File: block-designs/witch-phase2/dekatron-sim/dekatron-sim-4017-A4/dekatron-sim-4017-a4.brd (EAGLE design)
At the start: 27.9 x 27.9 mm, 19 parts, among them IC1 4017D, IC2 74LVC1G125DBV

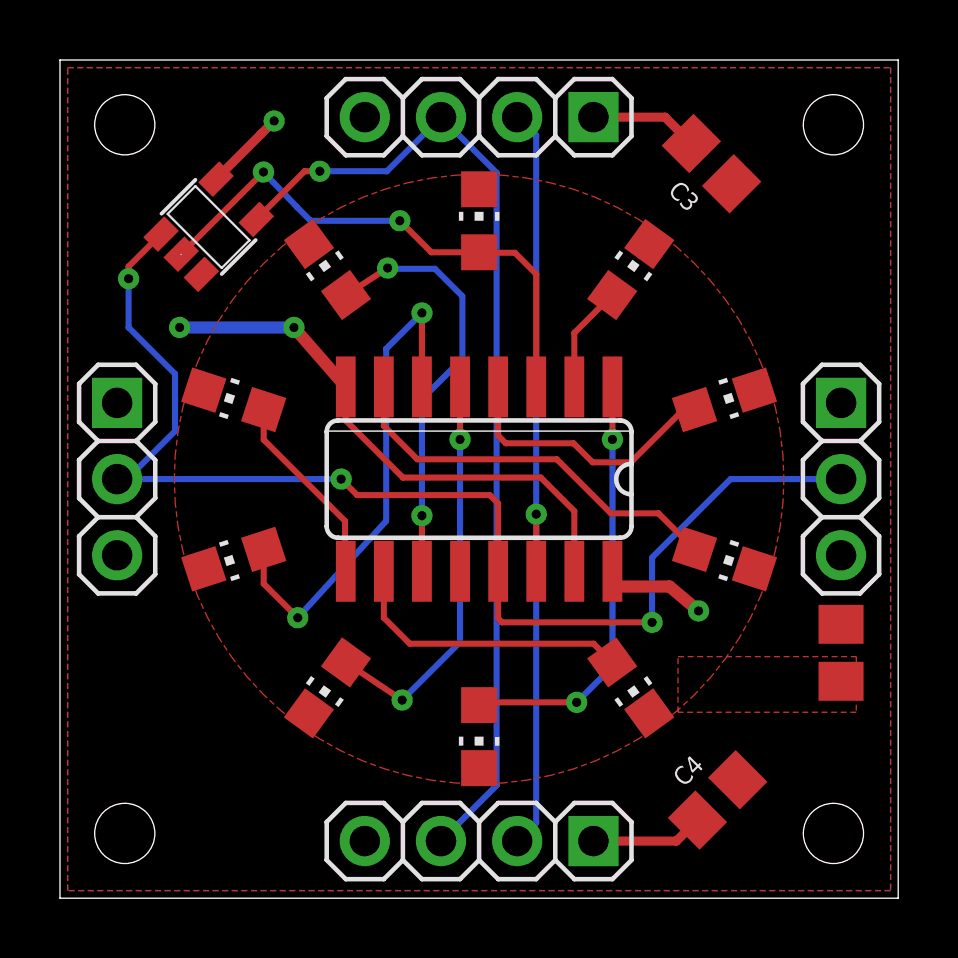
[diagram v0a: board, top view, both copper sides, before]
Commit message: updated designs for new labeling and spacing
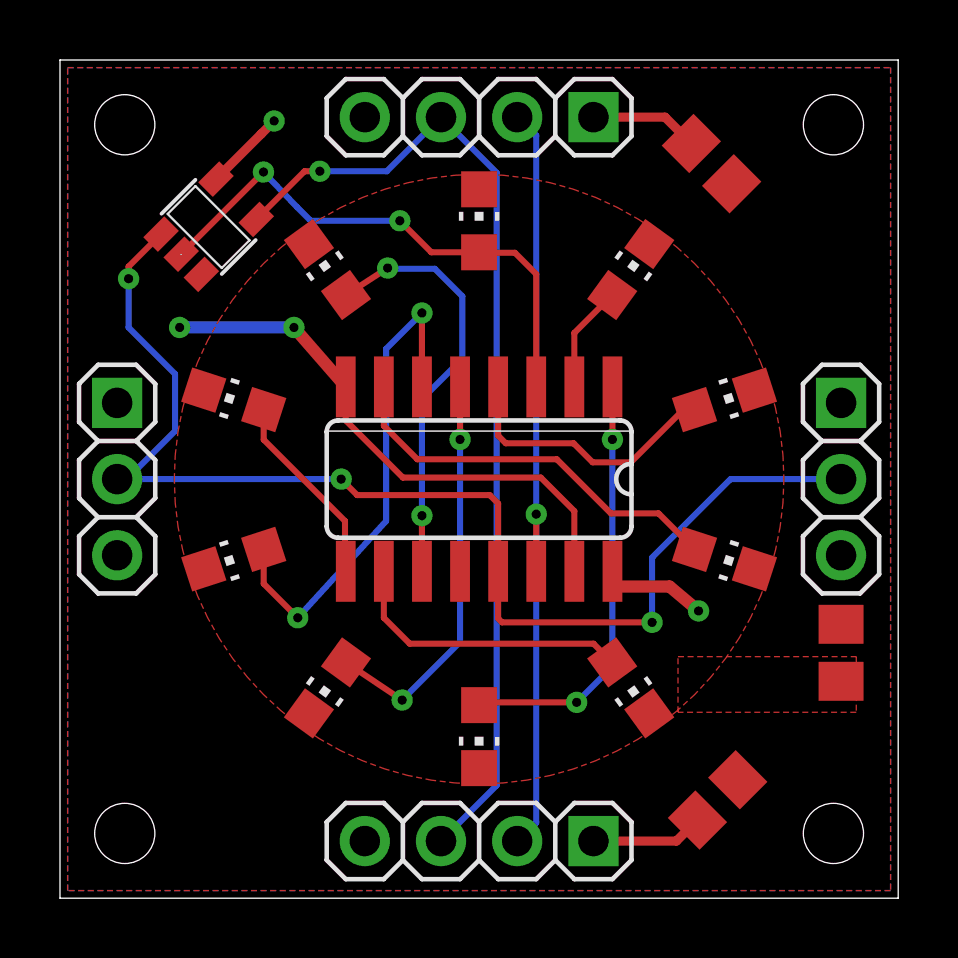
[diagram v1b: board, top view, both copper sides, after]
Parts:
- renumbered C3 to C1, C4 to C2, JP5 to JP1, JP6 to JP3
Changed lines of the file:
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@@
 <layer number="29" name="tStop" color="7" fill="3" visible="no" active="yes"/>
 <layer number="30" name="bStop" color="7" fill="6" visible="no" active="yes"/>
-<layer number="31" name="tCream" color="7" fill="4" visible="yes" active="yes"/>
+<layer number="31" name="tCream" color="7" fill="4" visible="no" active="yes"/>
 <layer number="32" name="bCream" color="7" fill="5" visible="no" active="yes"/>
 <layer number="33" name="tFinish" color="6" fill="3" visible="no" active="yes"/>
@@
 <wire x1="27.94" y1="0" x2="27.94" y2="27.94" width="0" layer="20"/>
 <circle x="13.97" y="13.97" radius="10.41994375" width="0.254" layer="51"/>
-<text x="13.5636" y="19.6342" size="1.016" layer="51">0</text>
-<text x="17.1958" y="18.6182" size="1.016" layer="51">1</text>
-<text x="19.5326" y="15.3416" size="1.016" layer="51">2</text>
-<text x="19.5326" y="11.3792" size="1.016" layer="51">3</text>
-<text x="17.1958" y="8.382" size="1.016" layer="51">4</text>
-<text x="13.5636" y="7.366" size="1.016" layer="51">5</text>
-<text x="10.0584" y="8.382" size="1.016" layer="51">6</text>
-<text x="7.6962" y="11.3792" size="1.016" layer="51">7</text>
-<text x="7.6962" y="15.3416" size="1.016" layer="51">8</text>
-<text x="10.0584" y="18.6182" size="1.016" layer="51">9</text>
+<text x="13.5636" y="19.558" size="1.016" layer="48">0</text>
+<text x="17.1958" y="18.415" size="1.016" layer="48">1</text>
+<text x="19.5326" y="15.3416" size="1.016" layer="48">2</text>
+<text x="19.5326" y="11.3792" size="1.016" layer="48">3</text>
+<text x="17.1958" y="8.509" size="1.016" layer="48">4</text>
+<text x="13.5636" y="7.493" size="1.016" layer="48">5</text>
+<text x="10.0584" y="8.509" size="1.016" layer="48">6</text>
+<text x="7.8232" y="11.3792" size="1.016" layer="48">7</text>
+<text x="7.8232" y="15.3416" size="1.016" layer="48">8</text>
+<text x="10.0584" y="18.415" size="1.016" layer="48">9</text>
 <hole x="2.159" y="2.159" drill="2.0066"/>
 <hole x="25.781" y="2.159" drill="2.0066"/>
@@
 <elements>
 <element name="IC1" library="40xx" package="SO16" value="4017D" x="13.97" y="13.97" smashed="yes" rot="R180">
-<attribute name="VALUE" x="9.745" y="17.22" size="0.6096" layer="27" rot="R270"/>
+<attribute name="VALUE" x="12.2948" y="13.7328" size="0.6096" layer="27"/>
 </element>
 <element name="LED1" library="led" package="CHIP-LED0805" value="RED" x="13.97" y="22.5806" smashed="yes"/>
@@
 <element name="LED9" library="led" package="CHIP-LED0805" value="RED" x="5.7912" y="16.6116" smashed="yes" rot="R72"/>
 <element name="LED10" library="led" package="CHIP-LED0805" value="RED" x="8.9154" y="20.955" smashed="yes" rot="R36"/>
-<element name="C3" library="resistor" package="C0805" value="" x="21.717" y="24.4856" smashed="yes" rot="R315">
-<attribute name="NAME" x="20.232003125" y="23.5466375" size="0.6096" layer="25" rot="R315"/>
+<element name="C1" library="resistor" package="C0805" value="" x="21.717" y="24.4856" smashed="yes" rot="R315">
 <attribute name="VALUE" x="19.4719375" y="23.49776875" size="1.27" layer="27" rot="R315"/>
 </element>
-<element name="C4" library="resistor" package="C0805" value="" x="21.9202" y="3.2766" smashed="yes" rot="R45">
-<attribute name="NAME" x="20.79621875" y="3.68035625" size="0.6096" layer="25" rot="R45"/>
+<element name="C2" library="resistor" package="C0805" value="" x="21.9202" y="3.2766" smashed="yes" rot="R45">
 <attribute name="VALUE" x="22.90803125" y="1.031534375" size="1.27" layer="27" rot="R45"/>
 </element>
 <element name="IC2" library="74xx-little-us" package="SOT23-5" value="74LVC1G125DBV" x="4.953" y="22.3774" smashed="yes" rot="R315">
-<attribute name="VALUE" x="1.360896875" y="22.377403125" size="1.27" layer="27" rot="R315"/>
+<attribute name="VALUE" x="4.927603125" y="25.004303125" size="0.3048" layer="27" rot="R225"/>
 </element>
 <element name="JP2" library="pinhead" package="1X04" value="" x="13.97" y="26.035" smashed="yes" rot="R180">
@@
 <attribute name="VALUE" x="23.494996875" y="8.8138" size="1.27" layer="27" rot="R270"/>
 </element>
-<element name="JP5" library="pinhead" package="1X03" value="" x="1.905" y="13.97" smashed="yes" rot="R270">
+<element name="JP1" library="pinhead" package="1X03" value="" x="1.905" y="13.97" smashed="yes" rot="R270">
 <attribute name="VALUE" x="-1.27" y="17.78" size="1.27" layer="27" rot="R270"/>
 </element>
-<element name="JP6" library="pinhead" package="1X03" value="" x="26.035" y="13.97" smashed="yes" rot="R270">
+<element name="JP3" library="pinhead" package="1X03" value="" x="26.035" y="13.97" smashed="yes" rot="R270">
 <attribute name="VALUE" x="22.86" y="17.78" size="1.27" layer="27" rot="R270"/>
 </element>
@@
 <signals>
 <signal name="GND">
-<contactref element="C3" pad="2"/>
-<contactref element="C4" pad="2"/>
+<contactref element="C1" pad="2"/>
+<contactref element="C2" pad="2"/>
 <contactref element="JP2" pad="4"/>
 <contactref element="JP4" pad="4"/>
@@
 </polygon>
 <contactref element="R1" pad="1"/>
-<contactref element="JP5" pad="3"/>
-<contactref element="JP6" pad="3"/>
+<contactref element="JP1" pad="3"/>
+<contactref element="JP3" pad="3"/>
 <contactref element="IC2" pad="3"/>
 <contactref element="IC1" pad="8"/>
@@
 <contactref element="IC1" pad="13"/>
 <contactref element="IC2" pad="1"/>
-<contactref element="JP5" pad="2"/>
-<contactref element="JP6" pad="2"/>
+<contactref element="JP1" pad="2"/>
+<contactref element="JP3" pad="2"/>
 <via x="2.286" y="20.6502" extent="1-16" drill="0.3048"/>
 <wire x1="2.7178" y1="13.97" x2="1.905" y2="13.97" width="0.2032" layer="16"/>
@@
 <signal name="VCC">
 <contactref element="IC2" pad="5"/>
-<contactref element="C4" pad="1"/>
-<contactref element="C3" pad="1"/>
+<contactref element="C2" pad="1"/>
+<contactref element="C1" pad="1"/>
 <polygon width="0.254" layer="16">
 <vertex x="27.686" y="0.254"/>
@@
 <vertex x="27.686" y="27.686"/>
 </polygon>
-<contactref element="JP5" pad="1"/>
-<contactref element="JP6" pad="1"/>
+<contactref element="JP1" pad="1"/>
+<contactref element="JP3" pad="1"/>
 <contactref element="JP2" pad="1"/>
 <contactref element="JP4" pad="1"/>

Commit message: add fiducials for pick-and-place
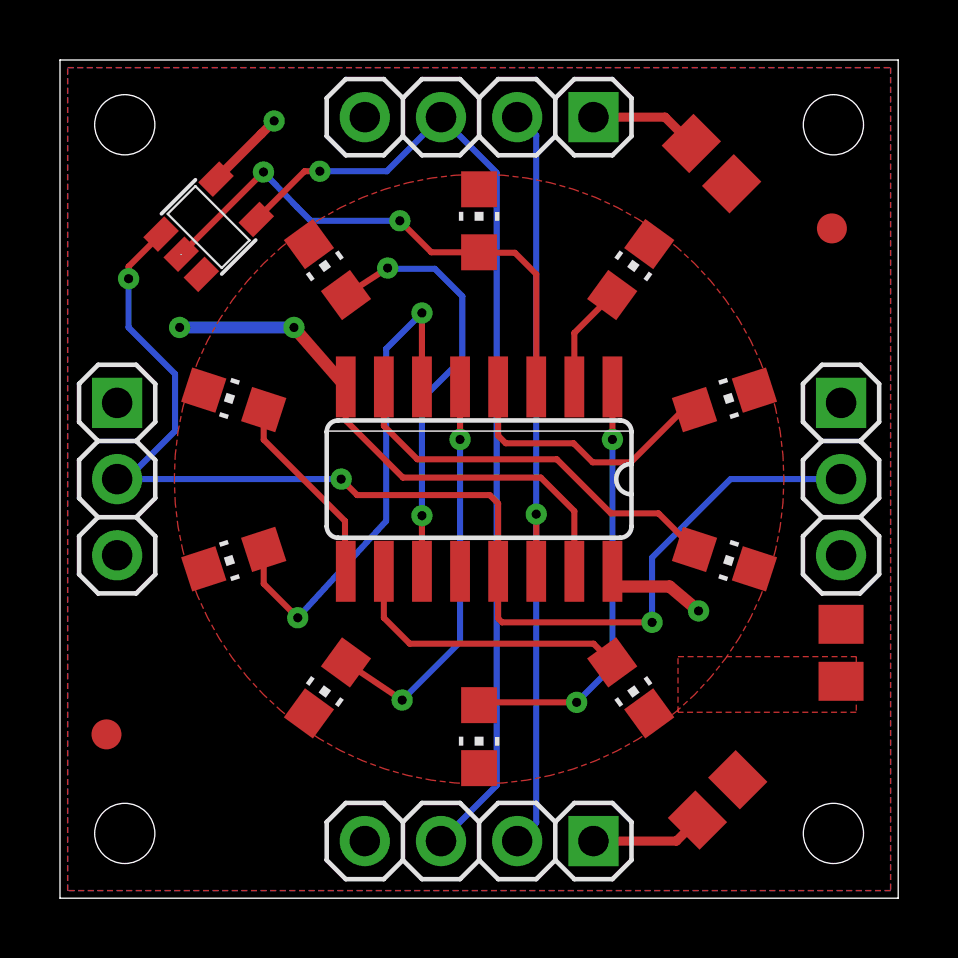
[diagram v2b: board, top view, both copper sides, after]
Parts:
- added FID1, FID2: FIDUCIAL, adafruit:FIDUCIAL_1MM
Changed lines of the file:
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@@
 <?xml version="1.0" encoding="utf-8"?>
 <!DOCTYPE eagle SYSTEM "eagle.dtd">
-<eagle version="7.3.0">
+<eagle version="7.6.0">
 <drawing>
 <settings>
@@
 <layer number="54" name="bGND_GNDA" color="1" fill="9" visible="no" active="no"/>
 <layer number="56" name="wert" color="7" fill="1" visible="no" active="no"/>
+<layer number="57" name="tCAD" color="7" fill="1" visible="no" active="no"/>
+<layer number="59" name="tCarbon" color="7" fill="1" visible="no" active="no"/>
+<layer number="60" name="bCarbon" color="7" fill="1" visible="no" active="no"/>
 <layer number="90" name="Modules" color="5" fill="1" visible="no" active="no"/>
 <layer number="91" name="Nets" color="2" fill="1" visible="no" active="no"/>
@@
 <layer number="106" name="bPlate" color="7" fill="1" visible="no" active="yes"/>
 <layer number="107" name="Crop" color="7" fill="1" visible="no" active="yes"/>
+<layer number="108" name="tplace-old" color="10" fill="1" visible="yes" active="yes"/>
+<layer number="109" name="ref-old" color="11" fill="1" visible="yes" active="yes"/>
+<layer number="110" name="fp0" color="7" fill="1" visible="yes" active="yes"/>
+<layer number="111" name="LPC17xx" color="7" fill="1" visible="yes" active="yes"/>
+<layer number="112" name="tSilk" color="7" fill="1" visible="yes" active="yes"/>
+<layer number="113" name="IDFDebug" color="7" fill="1" visible="yes" active="yes"/>
 <layer number="116" name="Patch_BOT" color="9" fill="4" visible="no" active="yes"/>
+<layer number="118" name="Rect_Pads" color="7" fill="1" visible="yes" active="yes"/>
 <layer number="121" name="_tsilk" color="7" fill="1" visible="no" active="yes"/>
 <layer number="122" name="_bsilk" color="7" fill="1" visible="no" active="yes"/>
+<layer number="123" name="tTestmark" color="7" fill="1" visible="yes" active="yes"/>
+<layer number="124" name="bTestmark" color="7" fill="1" visible="yes" active="yes"/>
 <layer number="125" name="_tNames" color="7" fill="1" visible="no" active="yes"/>
+<layer number="126" name="_bNames" color="7" fill="1" visible="yes" active="yes"/>
+<layer number="127" name="_tValues" color="7" fill="1" visible="yes" active="yes"/>
+<layer number="128" name="_bValues" color="7" fill="1" visible="yes" active="yes"/>
+<layer number="129" name="Mask" color="7" fill="1" visible="no" active="yes"/>
+<layer number="131" name="tAdjust" color="7" fill="1" visible="yes" active="yes"/>
+<layer number="132" name="bAdjust" color="7" fill="1" visible="yes" active="yes"/>
 <layer number="144" name="Drill_legend" color="7" fill="1" visible="no" active="yes"/>
+<layer number="145" name="DrillLegend_01-16" color="2" fill="9" visible="yes" active="yes"/>
+<layer number="150" name="Notes" color="7" fill="1" visible="yes" active="yes"/>
 <layer number="151" name="HeatSink" color="7" fill="1" visible="no" active="yes"/>
+<layer number="152" name="_bDocu" color="7" fill="1" visible="yes" active="yes"/>
+<layer number="153" name="FabDoc1" color="7" fill="1" visible="yes" active="yes"/>
+<layer number="154" name="FabDoc2" color="7" fill="1" visible="yes" active="yes"/>
+<layer number="155" name="FabDoc3" color="7" fill="1" visible="yes" active="yes"/>
+<layer number="199" name="Contour" color="7" fill="1" visible="yes" active="yes"/>
 <layer number="200" name="200bmp" color="1" fill="10" visible="no" active="yes"/>
 <layer number="201" name="201bmp" color="2" fill="10" visible="no" active="yes"/>
@@
 <layer number="223" name="223bmp" color="24" fill="1" visible="no" active="no"/>
 <layer number="224" name="224bmp" color="25" fill="1" visible="no" active="no"/>
+<layer number="225" name="225bmp" color="7" fill="1" visible="no" active="yes"/>
+<layer number="226" name="226bmp" color="7" fill="1" visible="no" active="yes"/>
+<layer number="227" name="227bmp" color="7" fill="1" visible="no" active="yes"/>
+<layer number="228" name="228bmp" color="7" fill="1" visible="no" active="yes"/>
+<layer number="229" name="229bmp" color="7" fill="1" visible="no" active="yes"/>
+<layer number="230" name="230bmp" color="7" fill="1" visible="no" active="yes"/>
+<layer number="231" name="231bmp" color="7" fill="1" visible="no" active="yes"/>
+<layer number="232" name="Eagle3D_PG2" color="7" fill="1" visible="no" active="no"/>
+<layer number="233" name="Eagle3D_PG3" color="7" fill="1" visible="no" active="no"/>
+<layer number="248" name="Housing" color="7" fill="1" visible="yes" active="yes"/>
+<layer number="249" name="Edge" color="7" fill="1" visible="yes" active="yes"/>
 <layer number="250" name="Descript" color="3" fill="1" visible="no" active="no"/>
 <layer number="251" name="SMDround" color="12" fill="11" visible="no" active="no"/>
 <layer number="254" name="cooling" color="7" fill="1" visible="no" active="yes"/>
+<layer number="255" name="routoute" color="7" fill="1" visible="yes" active="yes"/>
 </layers>
 <board>
@@
 <attribute name="VALUE" x="22.86" y="17.78" size="1.27" layer="27" rot="R270"/>
 </element>
+<element name="FID1" library="adafruit" package="FIDUCIAL_1MM" value="FIDUCIAL" x="25.7302" y="22.3266"/>
+<element name="FID2" library="adafruit" package="FIDUCIAL_1MM" value="FIDUCIAL" x="1.5494" y="5.461"/>
 </elements>
 <signals>
